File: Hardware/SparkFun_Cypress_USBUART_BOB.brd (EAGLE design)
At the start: 43.2 x 20.3 mm, 29 parts, among them J1 MICROB, J3 FTDI_BASICPTH, U1 CY7C65213, U2 MIC5219 3.3V

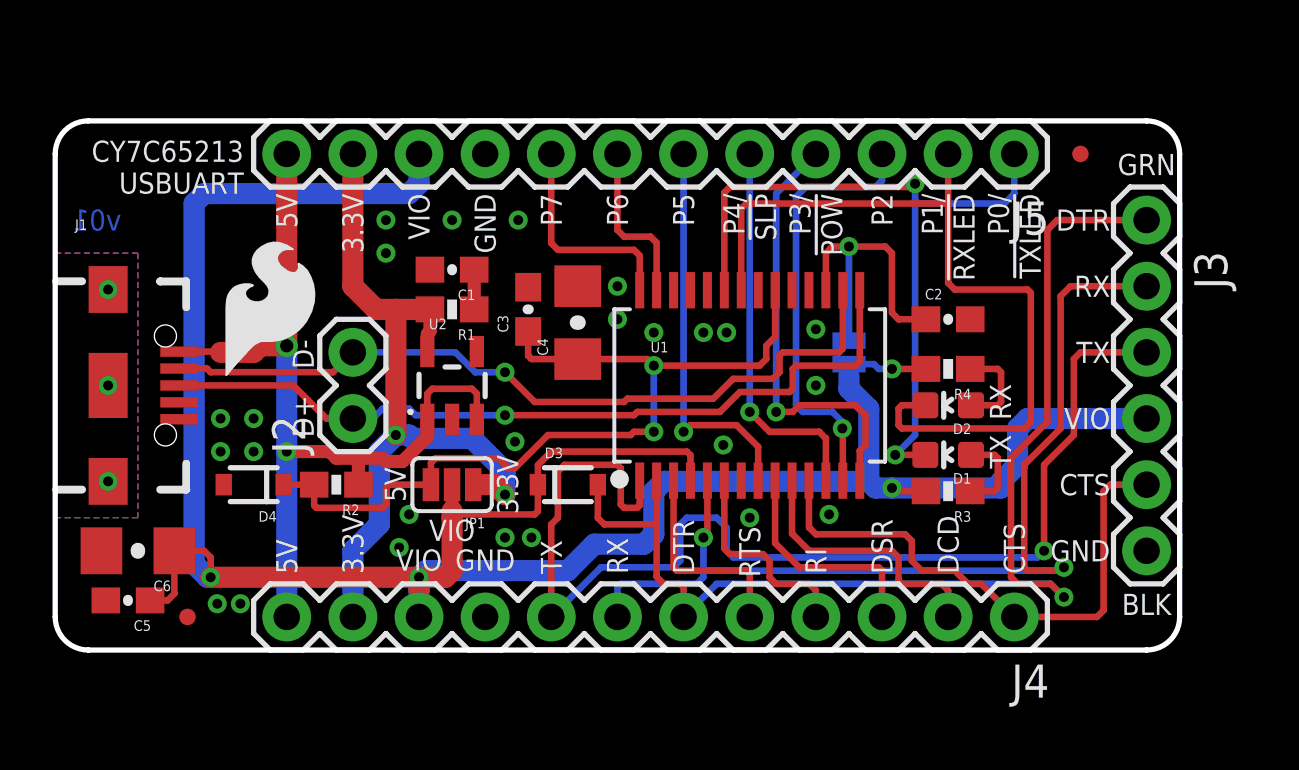
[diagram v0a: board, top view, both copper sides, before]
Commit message: Rotate a couple of parts, add 10k resistor, v02
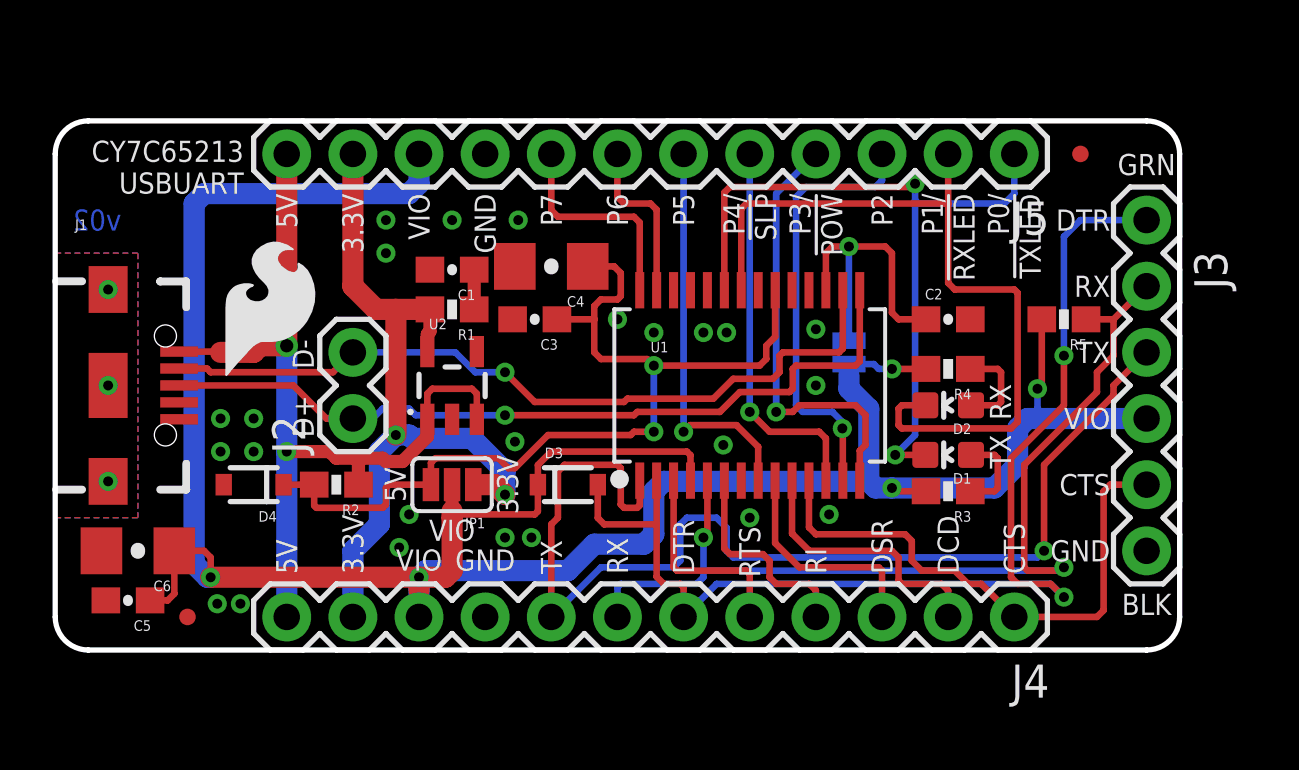
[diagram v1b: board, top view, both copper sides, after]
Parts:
- added R5: 10K, SparkFun-Resistors:0603-RES
- moved C4 2.39 mm to (19.1, 14.7), turned to 180 degrees
- moved C3 0.46 mm to (18.4, 12.7), turned to 180 degrees
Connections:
- net RXD: now also R5.1
- net VCCIO: now also R5.2
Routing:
- net VCCIO: track 99.4 -> 103.3 mm, vias 4 -> 5
- net 5V_CLAMPED: track 33.1 -> 36.3 mm
- net TXD: track 44.7 -> 43.3 mm
- net GPIO1: track 31.4 -> 30.3 mm
- net RXD: track 38.4 -> 37.7 mm
- net DTR: track 45.2 -> 44.7 mm, vias 1 -> 2
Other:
- board text added: "v02"
- board text removed: "v01"

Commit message: Changes from review incorporated
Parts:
- added FD3, FD4: FIDUCIALUFIDUCIAL, SparkFun-Aesthetics:MICRO-FIDUCIAL
- added R10, R11, R12, R13, R14, R15, R6, R7, R8, R9: 10K, SparkFun-Resistors:0603-RES
- U2: value MIC5219 3.3V -> 3.3V
- moved R5 9.11 mm to (31.8, 18.5), flipped to the bottom, turned to 270 degrees
- moved FD2 2.54 mm to (39.4, 21.6)
- moved J5 2.54 mm to (36.8, 21.6)
- moved C2 1.27 mm to (34.3, 14.0)
- moved C3 1.27 mm to (18.4, 14.0)
- moved R1 1.27 mm to (15.2, 14.4)
- moved D3 1.27 mm to (19.7, 7.62)
- moved D4 1.27 mm to (7.62, 7.62)
- moved R2 1.27 mm to (10.8, 7.62)
- moved C1 1.27 mm to (15.2, 15.9)
- moved C4 1.27 mm to (19.1, 16.0)
- moved D1 1.27 mm to (34.3, 8.76)
- moved D2 1.27 mm to (34.3, 10.7)
- moved FD1 1.27 mm to (6.35, 1.27)
- moved J1 1.27 mm to (2.03, 11.4)
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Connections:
- new net N$4: J1.ID1
- net CTS: now also R11.1
- net DCD: now also R12.1
- net DSR: now also R13.1
- net GPIO2: now also R5.1
- net GPIO3: now also R6.1
- net GPIO4: now also R7.1
- net GPIO5: now also R8.1
- net GPIO6: now also R9.1
- net GPIO7: now also R10.1
- net RI: now also R14.1
- net RXD: now also R15.1; no longer R5.1
- net VCCIO: now also R10.2, R11.2, R12.2, R13.2, R14.2, R15.2, R6.2, R7.2, R8.2, R9.2
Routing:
- net GPIO3: track 16.8 -> 33.2 mm, vias 1 -> 5
- net 5V: track 33.7 -> 41.3 mm
- net GPIO1: track 30.3 -> 23.7 mm, vias 0 -> 2
- net GPIO4: track 14.9 -> 20.8 mm, vias 1 -> 2
- net DCD: track 10.5 -> 16.4 mm, vias 0 -> 1
- net RTS: track 8.01 -> 13.6 mm, vias 0 -> 1
- net RI: track 8.18 -> 13.7 mm, vias 0 -> 1
- net DSR: track 8.72 -> 13.9 mm, vias 0 -> 2
- net GPIO6: track 6.45 -> 9.92 mm
- net GPIO7: track 8.35 -> 11.8 mm
- net GPIO0: track 28.6 -> 32.1 mm
- net TXD: track 43.3 -> 40.6 mm
- net 5V_CLAMPED: track 36.3 -> 33.7 mm
- net RXD: track 37.7 -> 40.3 mm, vias 2 -> 4
- net GPIO5: track 15.3 -> 17.6 mm, vias 1 -> 2
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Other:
- board size 43.2 x 20.3 mm -> 43.2 x 22.9 mm
- board text added: "CYPRESS CY7C65213 USBUART"
- board text added: "v03"
- board text removed: "CY7C65213 USBUART"
- board text removed: "v02"

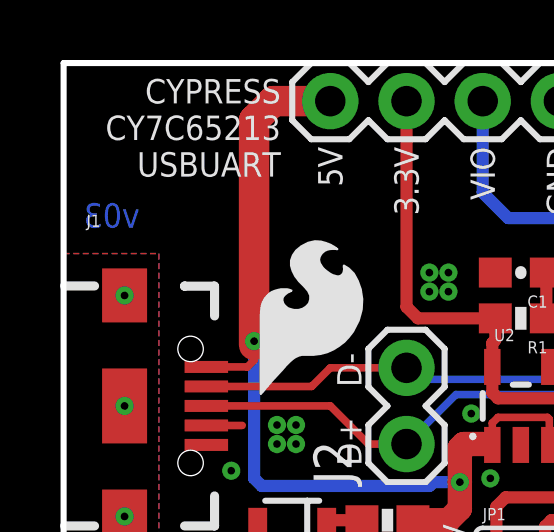
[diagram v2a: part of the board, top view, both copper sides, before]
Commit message: Changed version number for reds
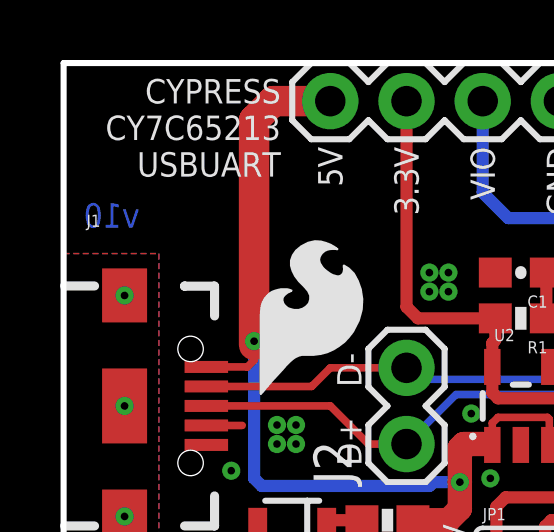
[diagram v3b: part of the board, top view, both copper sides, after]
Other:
- board text added: "v10"
- board text removed: "v03"
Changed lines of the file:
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@@
 <?xml version="1.0" encoding="utf-8"?>
 <!DOCTYPE eagle SYSTEM "eagle.dtd">
-<eagle version="7.5.0">
+<eagle version="7.6.0">
 <drawing>
 <settings>
@@
 <layer number="20" name="Dimension" color="15" fill="1" visible="yes" active="yes"/>
 <layer number="21" name="tPlace" color="16" fill="1" visible="yes" active="yes"/>
-<layer number="22" name="bPlace" color="14" fill="1" visible="no" active="yes"/>
+<layer number="22" name="bPlace" color="14" fill="1" visible="yes" active="yes"/>
 <layer number="23" name="tOrigins" color="15" fill="1" visible="yes" active="yes"/>
-<layer number="24" name="bOrigins" color="15" fill="1" visible="no" active="yes"/>
-<layer number="25" name="tNames" color="7" fill="1" visible="yes" active="yes"/>
+<layer number="24" name="bOrigins" color="15" fill="1" visible="yes" active="yes"/>
+<layer number="25" name="tNames" color="7" fill="1" visible="no" active="yes"/>
 <layer number="26" name="bNames" color="7" fill="1" visible="no" active="yes"/>
 <layer number="27" name="tValues" color="7" fill="1" visible="no" active="yes"/>
@@
 <layer number="43" name="vRestrict" color="2" fill="10" visible="no" active="yes"/>
 <layer number="44" name="Drills" color="7" fill="1" visible="no" active="yes"/>
-<layer number="45" name="Holes" color="7" fill="1" visible="no" active="yes"/>
+<layer number="45" name="Holes" color="7" fill="1" visible="yes" active="yes"/>
 <layer number="46" name="Milling" color="3" fill="1" visible="no" active="yes"/>
 <layer number="47" name="Measures" color="7" fill="1" visible="no" active="yes"/>
-<layer number="51" name="tDocu" color="6" fill="1" visible="no" active="yes"/>
+<layer number="51" name="tDocu" color="6" fill="1" visible="yes" active="yes"/>
 <layer number="52" name="bDocu" color="7" fill="1" visible="no" active="yes"/>
 <layer number="3" name="Route3" color="4" fill="3" visible="no" active="no"/>
@@
 CY7C65213
 USBUART</text>
-<text x="2.54" y="17.78" size="0.8128" layer="16" font="vector" ratio="15" rot="MR0" align="center-left">v03</text>
+<text x="2.54" y="17.78" size="0.8128" layer="16" font="vector" ratio="15" rot="MR0" align="center-left">v10</text>
 <text x="54.61" y="-17.78" size="1.778" layer="51" font="vector" ratio="10">Mike Hord</text>
 <dimension x1="0" y1="22.86" x2="0" y2="0" x3="-7.62" y3="11.43" textsize="1.778" textratio="10" layer="47" dtype="vertical" width="0.254" unit="inch"/>

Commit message: Revert to v02.
Revert "Changed version number for reds"

This reverts commit 640f5162c93cb70f6f1d384f505e534c75df1209.
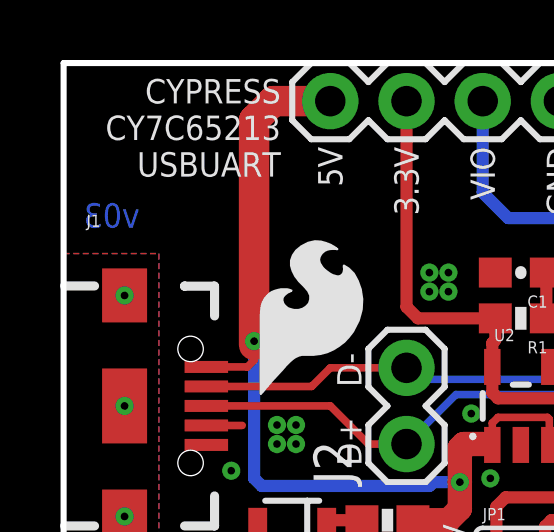
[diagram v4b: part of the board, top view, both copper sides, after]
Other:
- board text added: "v03"
- board text removed: "v10"
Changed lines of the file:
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@@
 <?xml version="1.0" encoding="utf-8"?>
 <!DOCTYPE eagle SYSTEM "eagle.dtd">
-<eagle version="7.6.0">
+<eagle version="7.5.0">
 <drawing>
 <settings>
@@
 <layer number="20" name="Dimension" color="15" fill="1" visible="yes" active="yes"/>
 <layer number="21" name="tPlace" color="16" fill="1" visible="yes" active="yes"/>
-<layer number="22" name="bPlace" color="14" fill="1" visible="yes" active="yes"/>
+<layer number="22" name="bPlace" color="14" fill="1" visible="no" active="yes"/>
 <layer number="23" name="tOrigins" color="15" fill="1" visible="yes" active="yes"/>
-<layer number="24" name="bOrigins" color="15" fill="1" visible="yes" active="yes"/>
-<layer number="25" name="tNames" color="7" fill="1" visible="no" active="yes"/>
+<layer number="24" name="bOrigins" color="15" fill="1" visible="no" active="yes"/>
+<layer number="25" name="tNames" color="7" fill="1" visible="yes" active="yes"/>
 <layer number="26" name="bNames" color="7" fill="1" visible="no" active="yes"/>
 <layer number="27" name="tValues" color="7" fill="1" visible="no" active="yes"/>
@@
 <layer number="43" name="vRestrict" color="2" fill="10" visible="no" active="yes"/>
 <layer number="44" name="Drills" color="7" fill="1" visible="no" active="yes"/>
-<layer number="45" name="Holes" color="7" fill="1" visible="yes" active="yes"/>
+<layer number="45" name="Holes" color="7" fill="1" visible="no" active="yes"/>
 <layer number="46" name="Milling" color="3" fill="1" visible="no" active="yes"/>
 <layer number="47" name="Measures" color="7" fill="1" visible="no" active="yes"/>
-<layer number="51" name="tDocu" color="6" fill="1" visible="yes" active="yes"/>
+<layer number="51" name="tDocu" color="6" fill="1" visible="no" active="yes"/>
 <layer number="52" name="bDocu" color="7" fill="1" visible="no" active="yes"/>
 <layer number="3" name="Route3" color="4" fill="3" visible="no" active="no"/>
@@
 CY7C65213
 USBUART</text>
-<text x="2.54" y="17.78" size="0.8128" layer="16" font="vector" ratio="15" rot="MR0" align="center-left">v10</text>
+<text x="2.54" y="17.78" size="0.8128" layer="16" font="vector" ratio="15" rot="MR0" align="center-left">v03</text>
 <text x="54.61" y="-17.78" size="1.778" layer="51" font="vector" ratio="10">Mike Hord</text>
 <dimension x1="0" y1="22.86" x2="0" y2="0" x3="-7.62" y3="11.43" textsize="1.778" textratio="10" layer="47" dtype="vertical" width="0.254" unit="inch"/>

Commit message: Revert to v02
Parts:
- removed FD3, FD4: FIDUCIALUFIDUCIAL, SparkFun-Aesthetics:MICRO-FIDUCIAL
- removed R10, R11, R12, R13, R14, R15, R6, R7, R8, R9: 10K, SparkFun-Resistors:0603-RES
- U2: value 3.3V -> MIC5219 3.3V
- moved R5 9.11 mm to (38.7, 12.7), flipped to the top, turned to 180 degrees
- moved FD2 2.54 mm to (39.4, 19.1)
- moved J5 2.54 mm to (36.8, 19.1)
- moved C2 1.27 mm to (34.3, 12.7)
- moved C3 1.27 mm to (18.4, 12.7)
- moved R1 1.27 mm to (15.2, 13.1)
- moved D3 1.27 mm to (19.7, 6.35)
- moved D4 1.27 mm to (7.62, 6.35)
- moved R2 1.27 mm to (10.8, 6.35)
- moved C1 1.27 mm to (15.2, 14.6)
- moved C4 1.27 mm to (19.1, 14.7)
- moved D1 1.27 mm to (34.3, 7.49)
- moved D2 1.27 mm to (34.3, 9.40)
- moved FD1 1.27 mm to (5.08, 1.27)
- moved J1 1.27 mm to (2.03, 10.2)
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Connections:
- removed net N$4: J1.ID1
- net CTS: no longer R11.1
- net DCD: no longer R12.1
- net DSR: no longer R13.1
- net GPIO2: no longer R5.1
- net GPIO3: no longer R6.1
- net GPIO4: no longer R7.1
- net GPIO5: no longer R8.1
- net GPIO6: no longer R9.1
- net GPIO7: no longer R10.1
- net RI: no longer R14.1
- net RXD: now also R5.1; no longer R15.1
- net VCCIO: no longer R10.2, R11.2, R12.2, R13.2, R14.2, R15.2, R6.2, R7.2, R8.2, R9.2
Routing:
- net GPIO3: track 33.2 -> 16.8 mm, vias 5 -> 1
- net 5V: track 41.3 -> 33.7 mm
- net GPIO1: track 23.7 -> 30.3 mm, vias 2 -> 0
- net GPIO4: track 20.8 -> 14.9 mm, vias 2 -> 1
- net DCD: track 16.4 -> 10.5 mm, vias 1 -> 0
- net RTS: track 13.6 -> 8.01 mm, vias 1 -> 0
- net RI: track 13.7 -> 8.18 mm, vias 1 -> 0
- net DSR: track 13.9 -> 8.72 mm, vias 2 -> 0
- net GPIO6: track 9.92 -> 6.45 mm
- net GPIO7: track 11.8 -> 8.35 mm
- net GPIO0: track 32.1 -> 28.6 mm
- net TXD: track 40.6 -> 43.3 mm
- net 5V_CLAMPED: track 33.7 -> 36.3 mm
- net RXD: track 40.3 -> 37.7 mm, vias 4 -> 2
- net GPIO5: track 17.6 -> 15.3 mm, vias 2 -> 1
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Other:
- board size 43.2 x 22.9 mm -> 43.2 x 20.3 mm
- board text added: "CY7C65213 USBUART"
- board text added: "v02"
- board text removed: "CYPRESS CY7C65213 USBUART"
- board text removed: "v03"

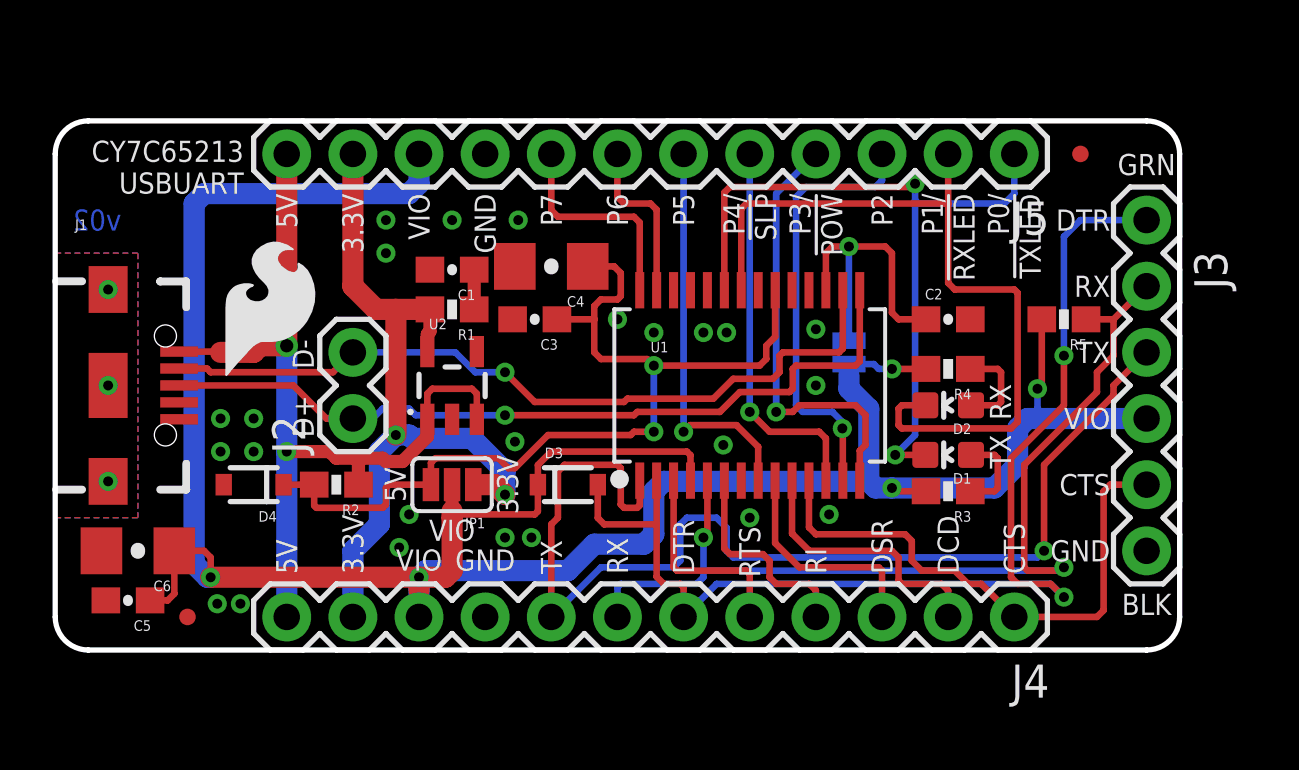
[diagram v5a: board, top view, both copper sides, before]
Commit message: Feedback from group review, add clamping diodes
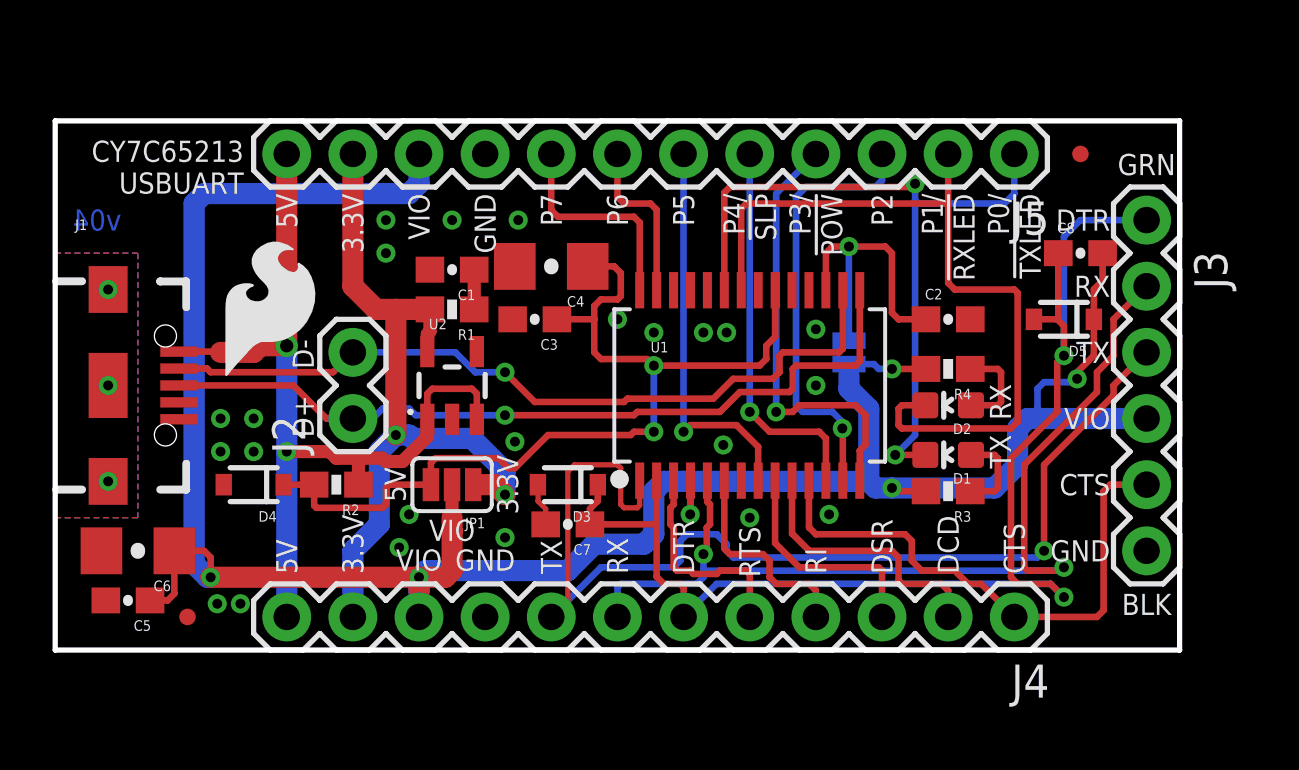
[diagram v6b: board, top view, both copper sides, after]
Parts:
- removed R5: 10K, SparkFun-Resistors:0603-RES
- added C7, C8: 10pF, SparkFun-Capacitors:0603-CAP
- added D5: PMEG4005EJ, SparkFun-DiscreteSemi:SOD-323
- U2: value MIC5219 3.3V -> 3.3V
- turned D3 to 180 degrees
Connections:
- net DTR: now also C7.1, C8.1, D3.C, D5.A; no longer D3.A
- net GND: now also C7.2, D3.A
- net RXD: no longer R5.1
- net VCCIO: now also C8.2, D5.C; no longer D3.C, R5.2
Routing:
- net DTR: track 44.7 -> 50.2 mm
- net VCCIO: track 103.3 -> 98.6 mm, vias 5 -> 6
- net GND: track 0.00 -> 1.52 mm, vias 24 -> 23
- net TXD: track 43.3 -> 41.8 mm
- net RXD: track 37.7 -> 36.7 mm
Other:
- outline, holes or cut-outs redrawn
- board text added: "v04"
- board text removed: "v02"
